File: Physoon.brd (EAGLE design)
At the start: 100 x 80 mm, 44 parts, among them IC2 74AHC1G125DBV, IC3 74AHC1G125DBV, M1 HX1, X1 BU-SMA-V

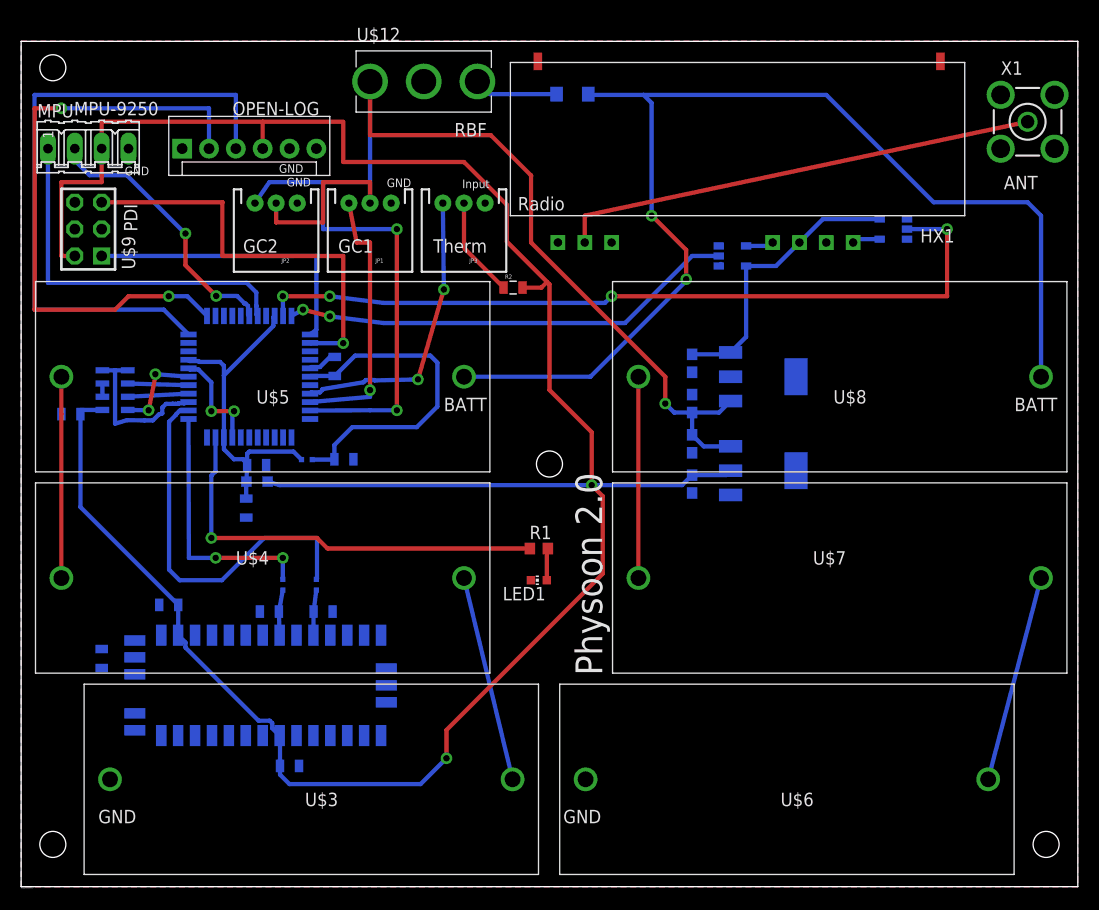
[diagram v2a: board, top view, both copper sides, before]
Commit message: Fix PDI
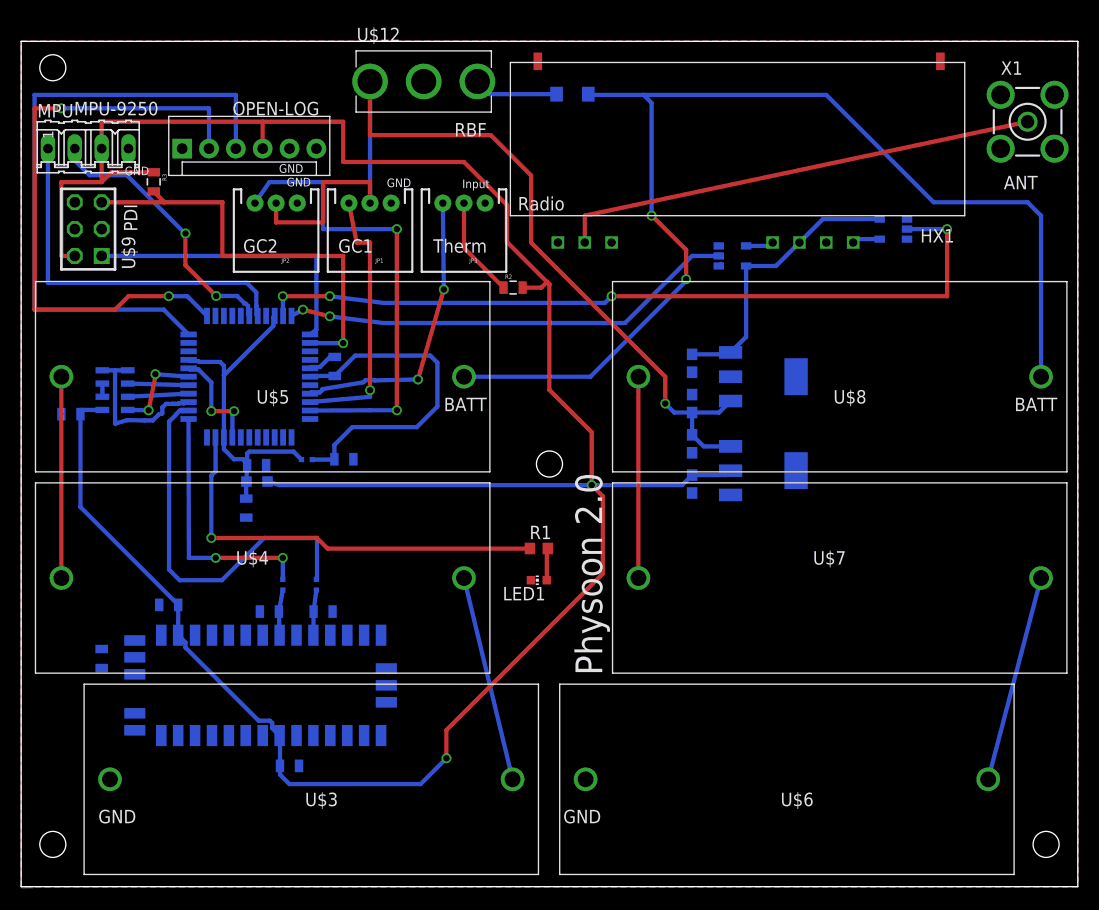
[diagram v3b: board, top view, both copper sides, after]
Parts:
- added R3: 50kOhm, SparkFun:0805
- L1: value (none) -> 10uH
- R2: value (none) -> 50kOhm
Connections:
- net PDI-CLK: now also R3.2
- net VCC: now also R3.1
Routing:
- net VCC: track 235.5 -> 240.9 mm
- net PDI-CLK: track 39.3 -> 40.8 mm
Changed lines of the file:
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@@
 </class>
 </classes>
-<designrules name="SparkFun">
-<description language="en">&lt;b&gt;EAGLE Design Rules&lt;/b&gt;
+<designrules name="LaenPCBOrder">
+<description language="de">&lt;b&gt;EAGLE Design Rules&lt;/b&gt;
 &lt;p&gt;
-The default Design Rules have been set to cover
-a wide range of applications. Your particular design
-may have different requirements, so please make the
-necessary adjustments and save your customized
-design rules under a new name.</description>
+Die Standard-Design-Rules sind so gewählt, dass sie für
+die meisten Anwendungen passen. Sollte ihre Platine
+besondere Anforderungen haben, treffen Sie die erforderlichen
+Einstellungen hier und speichern die Design Rules unter
+einem neuen Namen ab.</description>
+<description language="en">&lt;b&gt;Laen's PCB Order Design Rules&lt;/b&gt;
+&lt;p&gt;
+Please make sure your boards conform to these design rules.</description>
 <param name="layerSetup" value="(1*16)"/>
-<param name="mtCopper" value="0.035mm 0.035mm 0.035mm 0.035mm 0.035mm 0.035mm 0.035mm 0.035mm 0.035mm 0.035mm 0.035mm 0.035mm 0.035mm 0.035mm 0.035mm 0.035mm"/>
-<param name="mtIsolate" value="1.5mm 0.15mm 0.2mm 0.15mm 0.2mm 0.15mm 0.2mm 0.15mm 0.2mm 0.15mm 0.2mm 0.15mm 0.2mm 0.15mm 0.2mm"/>
-<param name="mdWireWire" value="8mil"/>
-<param name="mdWirePad" value="8mil"/>
-<param name="mdWireVia" value="8mil"/>
-<param name="mdPadPad" value="8mil"/>
-<param name="mdPadVia" value="8mil"/>
-<param name="mdViaVia" value="8mil"/>
-<param name="mdSmdPad" value="8mil"/>
-<param name="mdSmdVia" value="8mil"/>
-<param name="mdSmdSmd" value="8mil"/>
+<param name="mtCopper" value="0.0356mm 0.0356mm 0.0356mm 0.0356mm 0.0356mm 0.0356mm 0.0356mm 0.0356mm 0.0356mm 0.0356mm 0.0356mm 0.0356mm 0.0356mm 0.0356mm 0.0356mm 0.0356mm"/>
+<param name="mtIsolate" value="1.5011mm 0.1499mm 0.2007mm 0.1499mm 0.2007mm 0.1499mm 0.2007mm 0.1499mm 0.2007mm 0.1499mm 0.2007mm 0.1499mm 0.2007mm 0.1499mm 0.2007mm"/>
+<param name="mdWireWire" value="6mil"/>
+<param name="mdWirePad" value="6mil"/>
+<param name="mdWireVia" value="6mil"/>
+<param name="mdPadPad" value="6mil"/>
+<param name="mdPadVia" value="6mil"/>
+<param name="mdViaVia" value="6mil"/>
+<param name="mdSmdPad" value="6mil"/>
+<param name="mdSmdVia" value="6mil"/>
+<param name="mdSmdSmd" value="6mil"/>
 <param name="mdViaViaSameLayer" value="8mil"/>
 <param name="mnLayersViaInSmd" value="2"/>
-<param name="mdCopperDimension" value="8mil"/>
-<param name="mdDrill" value="8mil"/>
+<param name="mdCopperDimension" value="15mil"/>
+<param name="mdDrill" value="6mil"/>
 <param name="mdSmdStop" value="0mil"/>
-<param name="msWidth" value="8mil"/>
-<param name="msDrill" value="20mil"/>
-<param name="msMicroVia" value="9.99mm"/>
+<param name="msWidth" value="6mil"/>
+<param name="msDrill" value="13mil"/>
+<param name="msMicroVia" value="13mil"/>
 <param name="msBlindViaRatio" value="0.5"/>
 <param name="rvPadTop" value="0.25"/>
@@
 <param name="rvMicroViaOuter" value="0.25"/>
 <param name="rvMicroViaInner" value="0.25"/>
-<param name="rlMinPadTop" value="12mil"/>
+<param name="rlMinPadTop" value="7mil"/>
 <param name="rlMaxPadTop" value="20mil"/>
-<param name="rlMinPadInner" value="10mil"/>
+<param name="rlMinPadInner" value="7mil"/>
 <param name="rlMaxPadInner" value="20mil"/>
-<param name="rlMinPadBottom" value="12mil"/>
+<param name="rlMinPadBottom" value="7mil"/>
 <param name="rlMaxPadBottom" value="20mil"/>
-<param name="rlMinViaOuter" value="10mil"/>
+<param name="rlMinViaOuter" value="7mil"/>
 <param name="rlMaxViaOuter" value="20mil"/>
-<param name="rlMinViaInner" value="10mil"/>
+<param name="rlMinViaInner" value="7mil"/>
 <param name="rlMaxViaInner" value="20mil"/>
 <param name="rlMinMicroViaOuter" value="4mil"/>
@@
 <param name="mvStopFrame" value="1"/>
 <param name="mvCreamFrame" value="0"/>
-<param name="mlMinStopFrame" value="4mil"/>
-<param name="mlMaxStopFrame" value="4mil"/>
+<param name="mlMinStopFrame" value="3mil"/>
+<param name="mlMaxStopFrame" value="3mil"/>
 <param name="mlMinCreamFrame" value="0mil"/>
 <param name="mlMaxCreamFrame" value="0mil"/>
-<param name="mlViaStopLimit" value="20mil"/>
+<param name="mlViaStopLimit" value="0mil"/>
 <param name="srRoundness" value="0"/>
 <param name="srMinRoundness" value="0mil"/>
@@
 <element name="R1" library="resistor" package="R0603" value="220" x="49" y="32"/>
 <element name="DIODE" library="Physoon" package="LILYPAD-WEARABLES_LED-1206" value="" x="52.17348125" y="75.005" rot="MR0"/>
-<element name="R2" library="SparkFun" package="0805" value="" x="46.558196875" y="56.695340625"/>
-<element name="L1" library="rcl" library_urn="urn:adsk.eagle:library:334" package="L2012C" value="" x="22.321515625" y="38.336221875" rot="MR180"/>
+<element name="R2" library="SparkFun" package="0805" value="50kOhm" x="46.558196875" y="56.695340625"/>
+<element name="L1" library="rcl" library_urn="urn:adsk.eagle:library:334" package="L2012C" value="10uH" x="22.321515625" y="38.336221875" rot="MR180"/>
 <element name="C11" library="SparkFun" package="0805" value="10uF" x="22.288503125" y="39.888159375" rot="MR180"/>
 <element name="L2" library="rc-master-smd" package="L0402" value="FB_0402" x="27.04338125" y="40.416478125" rot="MR0"/>
@@
 <element name="C16" library="SparkFun" package="0805" value="100nF" x="29.68496875" y="49.232825" rot="MR270"/>
 <element name="C12" library="SparkFun" package="0805" value="100nF" x="21.2979" y="35.826703125" rot="MR270"/>
+<element name="R3" library="SparkFun" package="0805" value="50kOhm" x="12.547603125" y="66.7004" rot="R270"/>
 </elements>
 <signals>
@@
 <contactref element="IC1" pad="35"/>
 <contactref element="U$9" pad="5"/>
-<wire x1="7.62" y1="64.77" x2="19.05" y2="64.77" width="0.4064" layer="1"/>
+<wire x1="13.5382" y1="64.77" x2="7.62" y2="64.77" width="0.4064" layer="1"/>
+<wire x1="13.5382" y1="64.77" x2="19.05" y2="64.77" width="0.4064" layer="1"/>
 <wire x1="19.05" y1="64.77" x2="19.05" y2="59.69" width="0.4064" layer="1"/>
 <wire x1="19.05" y1="59.69" x2="30.48" y2="59.69" width="0.4064" layer="1"/>
@@
 <wire x1="30.48" y1="51.435" x2="27.365" y2="51.435" width="0.4064" layer="16"/>
 <wire x1="27.365" y1="51.435" x2="27.34" y2="51.46" width="0.4064" layer="16"/>
+<contactref element="R3" pad="2"/>
+<wire x1="12.547603125" y1="65.8004" x2="13.5382" y2="64.809803125" width="0.4064" layer="1"/>
+<wire x1="13.5382" y1="64.809803125" x2="13.5382" y2="64.77" width="0.4064" layer="1"/>
 </signal>
 <signal name="VCC">
@@
 <wire x1="55.044340625" y1="29.618940625" x2="55.044340625" y2="36.955659375" width="0.4064" layer="1"/>
 <wire x1="55.044340625" y1="36.955659375" x2="54" y2="38" width="0.4064" layer="1"/>
+<contactref element="R3" pad="1"/>
+<wire x1="7.62" y1="66.675" x2="8.5454" y2="67.6004" width="0.4064" layer="1"/>
+<wire x1="8.5454" y1="67.6004" x2="12.547603125" y2="67.6004" width="0.4064" layer="1"/>
 </signal>
 <signal name="N$1">
